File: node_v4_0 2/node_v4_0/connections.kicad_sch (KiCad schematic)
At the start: 11 parts, among them J4 Conn_02x08_Odd_Even, J5 Conn_02x02_Odd_Even, J6 GNSS_ANT, J7 RF_ANT

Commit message: most routing done
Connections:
- net GP6 renamed GP27
- net GP7 renamed GP28
- net GP8 renamed GP29
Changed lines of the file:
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@@
 		)
 	)
-	(global_label "GP7"
+	(global_label "SCL"
+		(shape input)
+		(at 120.65 107.95 0)
+		(fields_autoplaced yes)
+		(effects
+			(font
+				(size 1.27 1.27)
+			)
+			(justify left)
+		)
+		(property "Intersheetrefs" "${INTERSHEET_REFS}"
+			(at 127.1428 107.95 0)
+			(effects
+				(font
+					(size 1.27 1.27)
+				)
+				(justify left)
+				(hide yes)
+			)
+		)
+	)
+	(global_label "MOSI"
+		(shape input)
+		(at 105.41 100.33 180)
+		(fields_autoplaced yes)
+		(effects
+			(font
+				(size 1.27 1.27)
+			)
+			(justify right)
+		)
+		(property "Intersheetrefs" "${INTERSHEET_REFS}"
+			(at 97.8286 100.33 0)
+			(effects
+				(font
+					(size 1.27 1.27)
+				)
+				(justify right)
+				(hide yes)
+			)
+		)
+	)
+	(global_label "SWD"
+		(shape input)
+		(at 105.41 64.77 180)
+		(fields_autoplaced yes)
+		(effects
+			(font
+				(size 1.27 1.27)
+			)
+			(justify right)
+		)
+		(property "Intersheetrefs" "${INTERSHEET_REFS}"
+			(at 98.4939 64.77 0)
+			(effects
+				(font
+					(size 1.27 1.27)
+				)
+				(justify right)
+				(hide yes)
+			)
+		)
+	)
+	(global_label "MISO"
+		(shape input)
+		(at 105.41 102.87 180)
+		(fields_autoplaced yes)
+		(effects
+			(font
+				(size 1.27 1.27)
+			)
+			(justify right)
+		)
+		(property "Intersheetrefs" "${INTERSHEET_REFS}"
+			(at 97.8286 102.87 0)
+			(effects
+				(font
+					(size 1.27 1.27)
+				)
+				(justify right)
+				(hide yes)
+			)
+		)
+	)
+	(global_label "GNSS_ANT"
+		(shape input)
+		(at 185.42 78.74 180)
+		(fields_autoplaced yes)
+		(effects
+			(font
+				(size 1.27 1.27)
+			)
+			(justify right)
+		)
+		(property "Intersheetrefs" "${INTERSHEET_REFS}"
+			(at 173.061 78.74 0)
+			(effects
+				(font
+					(size 1.27 1.27)
+				)
+				(justify right)
+				(hide yes)
+			)
+		)
+	)
+	(global_label "SPI_CS"
+		(shape input)
+		(at 105.41 107.95 180)
+		(fields_autoplaced yes)
+		(effects
+			(font
+				(size 1.27 1.27)
+			)
+			(justify right)
+		)
+		(property "Intersheetrefs" "${INTERSHEET_REFS}"
+			(at 95.8934 107.95 0)
+			(effects
+				(font
+					(size 1.27 1.27)
+				)
+				(justify right)
+				(hide yes)
+			)
+		)
+	)
+	(global_label "RF_ANT"
+		(shape input)
+		(at 196.85 121.92 180)
+		(fields_autoplaced yes)
+		(effects
+			(font
+				(size 1.27 1.27)
+			)
+			(justify right)
+		)
+		(property "Intersheetrefs" "${INTERSHEET_REFS}"
+			(at 187.1519 121.92 0)
+			(effects
+				(font
+					(size 1.27 1.27)
+				)
+				(justify right)
+				(hide yes)
+			)
+		)
+	)
+	(global_label "TX1"
+		(shape input)
+		(at 105.41 95.25 180)
+		(fields_autoplaced yes)
+		(effects
+			(font
+				(size 1.27 1.27)
+			)
+			(justify right)
+		)
+		(property "Intersheetrefs" "${INTERSHEET_REFS}"
+			(at 99.0382 95.25 0)
+			(effects
+				(font
+					(size 1.27 1.27)
+				)
+				(justify right)
+				(hide yes)
+			)
+		)
+	)
+	(global_label "GP28"
 		(shape input)
 		(at 120.65 100.33 0)
@@
 		)
 		(property "Intersheetrefs" "${INTERSHEET_REFS}"
-			(at 127.3847 100.33 0)
-			(effects
-				(font
-					(size 1.27 1.27)
-				)
-				(justify left)
-				(hide yes)
-			)
-		)
-	)
-	(global_label "GP6"
+			(at 128.5942 100.33 0)
+			(effects
+				(font
+					(size 1.27 1.27)
+				)
+				(justify left)
+				(hide yes)
+			)
+		)
+	)
+	(global_label "GP29"
+		(shape input)
+		(at 120.65 102.87 0)
+		(fields_autoplaced yes)
+		(effects
+			(font
+				(size 1.27 1.27)
+			)
+			(justify left)
+		)
+		(property "Intersheetrefs" "${INTERSHEET_REFS}"
+			(at 128.5942 102.87 0)
+			(effects
+				(font
+					(size 1.27 1.27)
+				)
+				(justify left)
+				(hide yes)
+			)
+		)
+	)
+	(global_label "SDA"
+		(shape input)
+		(at 120.65 105.41 0)
+		(fields_autoplaced yes)
+		(effects
+			(font
+				(size 1.27 1.27)
+			)
+			(justify left)
+		)
+		(property "Intersheetrefs" "${INTERSHEET_REFS}"
+			(at 127.2033 105.41 0)
+			(effects
+				(font
+					(size 1.27 1.27)
+				)
+				(justify left)
+				(hide yes)
+			)
+		)
+	)
+	(global_label "GP27"
 		(shape input)
 		(at 120.65 97.79 0)
@@
 		)
 		(property "Intersheetrefs" "${INTERSHEET_REFS}"
-			(at 127.3847 97.79 0)
-			(effects
-				(font
-					(size 1.27 1.27)
-				)
-				(justify left)
-				(hide yes)
-			)
-		)
-	)
-	(global_label "SCL"
-		(shape input)
-		(at 120.65 107.95 0)
-		(fields_autoplaced yes)
-		(effects
-			(font
-				(size 1.27 1.27)
-			)
-			(justify left)
-		)
-		(property "Intersheetrefs" "${INTERSHEET_REFS}"
-			(at 127.1428 107.95 0)
-			(effects
-				(font
-					(size 1.27 1.27)
-				)
-				(justify left)
-				(hide yes)
-			)
-		)
-	)
-	(global_label "MOSI"
-		(shape input)
-		(at 105.41 100.33 180)
-		(fields_autoplaced yes)
-		(effects
-			(font
-				(size 1.27 1.27)
-			)
-			(justify right)
-		)
-		(property "Intersheetrefs" "${INTERSHEET_REFS}"
-			(at 97.8286 100.33 0)
-			(effects
-				(font
-					(size 1.27 1.27)
-				)
-				(justify right)
-				(hide yes)
-			)
-		)
-	)
-	(global_label "SWD"
-		(shape input)
-		(at 105.41 64.77 180)
-		(fields_autoplaced yes)
-		(effects
-			(font
-				(size 1.27 1.27)
-			)
-			(justify right)
-		)
-		(property "Intersheetrefs" "${INTERSHEET_REFS}"
-			(at 98.4939 64.77 0)
-			(effects
-				(font
-					(size 1.27 1.27)
-				)
-				(justify right)
-				(hide yes)
-			)
-		)
-	)
-	(global_label "MISO"
-		(shape input)
-		(at 105.41 102.87 180)
-		(fields_autoplaced yes)
-		(effects
-			(font
-				(size 1.27 1.27)
-			)
-			(justify right)
-		)
-		(property "Intersheetrefs" "${INTERSHEET_REFS}"
-			(at 97.8286 102.87 0)
-			(effects
-				(font
-					(size 1.27 1.27)
-				)
-				(justify right)
-				(hide yes)
-			)
-		)
-	)
-	(global_label "GNSS_ANT"
-		(shape input)
-		(at 185.42 78.74 180)
-		(fields_autoplaced yes)
-		(effects
-			(font
-				(size 1.27 1.27)
-			)
-			(justify right)
-		)
-		(property "Intersheetrefs" "${INTERSHEET_REFS}"
-			(at 173.061 78.74 0)
-			(effects
-				(font
-					(size 1.27 1.27)
-				)
-				(justify right)
-				(hide yes)
-			)
-		)
-	)
-	(global_label "SPI_CS"
-		(shape input)
-		(at 105.41 107.95 180)
-		(fields_autoplaced yes)
-		(effects
-			(font
-				(size 1.27 1.27)
-			)
-			(justify right)
-		)
-		(property "Intersheetrefs" "${INTERSHEET_REFS}"
-			(at 95.8934 107.95 0)
-			(effects
-				(font
-					(size 1.27 1.27)
-				)
-				(justify right)
-				(hide yes)
-			)
-		)
-	)
-	(global_label "RF_ANT"
-		(shape input)
-		(at 196.85 121.92 180)
-		(fields_autoplaced yes)
-		(effects
-			(font
-				(size 1.27 1.27)
-			)
-			(justify right)
-		)
-		(property "Intersheetrefs" "${INTERSHEET_REFS}"
-			(at 187.1519 121.92 0)
-			(effects
-				(font
-					(size 1.27 1.27)
-				)
-				(justify right)
-				(hide yes)
-			)
-		)
-	)
-	(global_label "TX1"
-		(shape input)
-		(at 105.41 95.25 180)
-		(fields_autoplaced yes)
-		(effects
-			(font
-				(size 1.27 1.27)
-			)
-			(justify right)
-		)
-		(property "Intersheetrefs" "${INTERSHEET_REFS}"
-			(at 99.0382 95.25 0)
-			(effects
-				(font
-					(size 1.27 1.27)
-				)
-				(justify right)
-				(hide yes)
-			)
-		)
-	)
-	(global_label "GP8"
-		(shape input)
-		(at 120.65 102.87 0)
-		(fields_autoplaced yes)
-		(effects
-			(font
-				(size 1.27 1.27)
-			)
-			(justify left)
-		)
-		(property "Intersheetrefs" "${INTERSHEET_REFS}"
-			(at 127.3847 102.87 0)
-			(effects
-				(font
-					(size 1.27 1.27)
-				)
-				(justify left)
-				(hide yes)
-			)
-		)
-	)
-	(global_label "SDA"
-		(shape input)
-		(at 120.65 105.41 0)
-		(fields_autoplaced yes)
-		(effects
-			(font
-				(size 1.27 1.27)
-			)
-			(justify left)
-		)
-		(property "Intersheetrefs" "${INTERSHEET_REFS}"
-			(at 127.2033 105.41 0)
-			(effects
-				(font
+			(at 128.5942 97.79 0)
+			(effects
+				(font

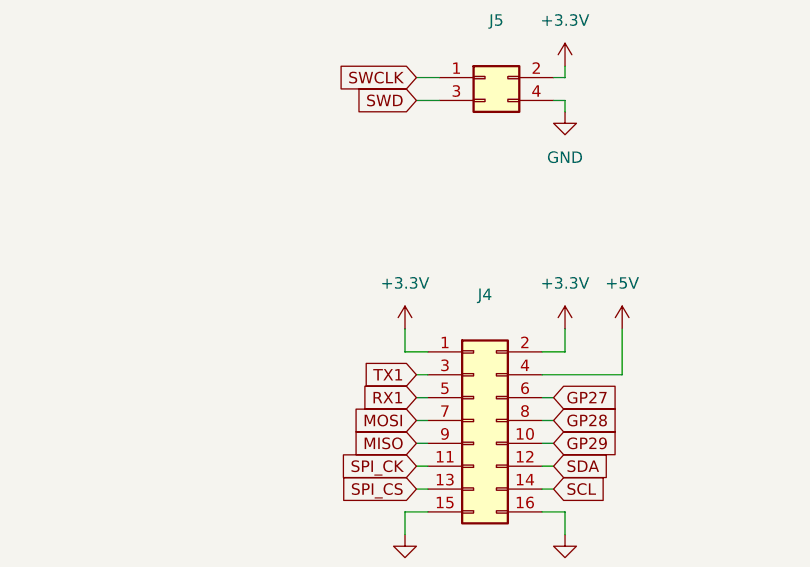
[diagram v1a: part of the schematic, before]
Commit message: added vin for solar/charge, more minor fixes
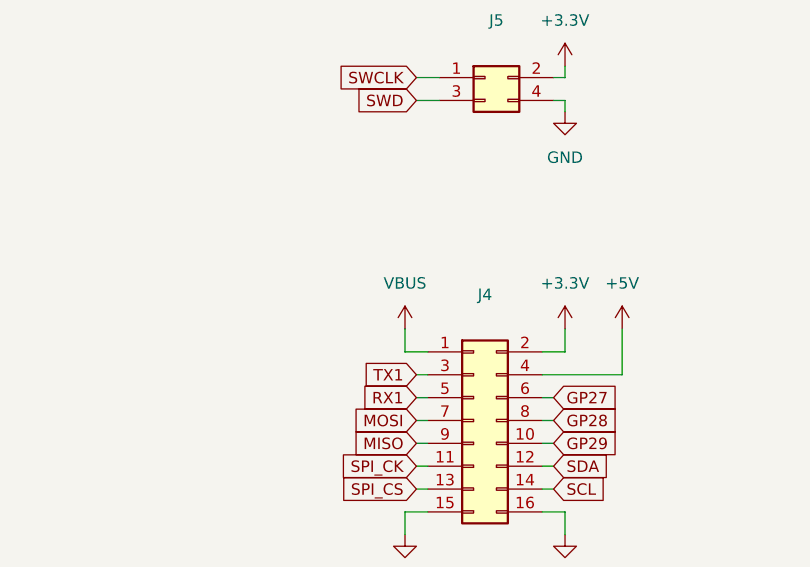
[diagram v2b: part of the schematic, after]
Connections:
- net +3.3V: no longer J4.1 (Pin_1)
- new net VBUS: J4.1 (Pin_1)
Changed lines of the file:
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@@
+	)
+	(symbol
+		(lib_id "power:VBUS")
+		(at 104.14 90.17 0)
+		(unit 1)
+		(exclude_from_sim no)
+		(in_bom yes)
+		(on_board yes)
+		(dnp no)
+		(fields_autoplaced yes)
+		(property "Reference" "#PWR055"
+			(at 104.14 93.98 0)
+			(effects
+				(font
+					(size 1.27 1.27)
+				)
+				(hide yes)
+			)
+		)
+		(property "Value" "VBUS"
+			(at 104.14 85.09 0)
+			(effects
+				(font
+					(size 1.27 1.27)
+				)
+			)
+		)
+		(property "Footprint" ""
+			(at 104.14 90.17 0)
+			(effects
+				(font
+					(size 1.27 1.27)
+				)
+				(hide yes)
+			)
+		)
+		(property "Datasheet" ""
+			(at 104.14 90.17 0)
+			(effects
+				(font
+					(size 1.27 1.27)
+				)
+				(hide yes)
+			)
+		)
+		(property "Description" "Power symbol creates a global label with name \"VBUS\""
+			(at 104.14 90.17 0)
+			(effects
+				(font
+					(size 1.27 1.27)
+				)
+				(hide yes)
+			)
+		)
+		(pin "1"
+		)
+		(instances
+			(project "node_v4_0"
+				(path "/03dc898e-8f05-4377-b5c6-8a0f09836da8/acf22234-ba16-4d6b-83f4-1166d3ac6600"
+					(reference "#PWR055")
+					(unit 1)
+				)
+			)
+		)
 	)
 	(symbol
@@
 					(unit 1)
 				)
-			)
-		)
-	)
-	(symbol
-		(lib_id "power:+3.3V")
-		(at 104.14 90.17 0)
-		(unit 1)
-		(exclude_from_sim no)
-		(in_bom yes)
-		(on_board yes)
-		(dnp no)
-		(fields_autoplaced yes)
-		(property "Reference" "#PWR055"
-			(at 104.14 93.98 0)
-			(effects
-				(font
-					(size 1.27 1.27)
-				)
-				(hide yes)
-			)
-		)
-		(property "Value" "+3.3V"
-			(at 104.14 85.09 0)
-			(effects
-				(font
-					(size 1.27 1.27)
-				)
-			)
-		)
-		(property "Footprint" ""
-			(at 104.14 90.17 0)
-			(effects
-				(font
-					(size 1.27 1.27)
-				)
-				(hide yes)
-			)
-		)
-		(property "Datasheet" ""
-			(at 104.14 90.17 0)
-			(effects
-				(font
-					(size 1.27 1.27)
-				)
-				(hide yes)
-			)
-		)
-		(property "Description" "Power symbol creates a global label with name \"+3.3V\""
-			(at 104.14 90.17 0)
-			(effects
-				(font
-					(size 1.27 1.27)
-				)
-				(hide yes)
-			)
-		)
-		(pin "1"
-		)
-		(instances
-			(project "node_v4_0"
-				(path "/03dc898e-8f05-4377-b5c6-8a0f09836da8/acf22234-ba16-4d6b-83f4-1166d3ac6600"
-					(reference "#PWR055")
-					(unit 1)
-				)

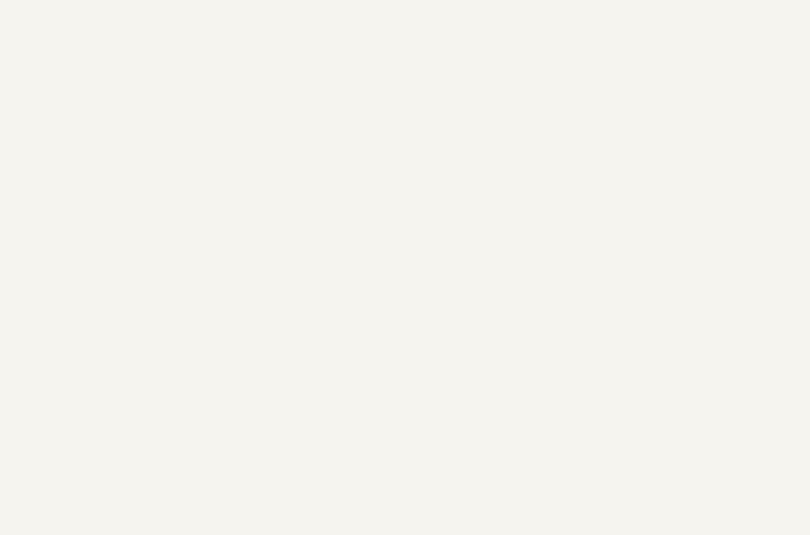
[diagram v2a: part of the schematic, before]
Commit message: moved reset button to make space for vin jst connector
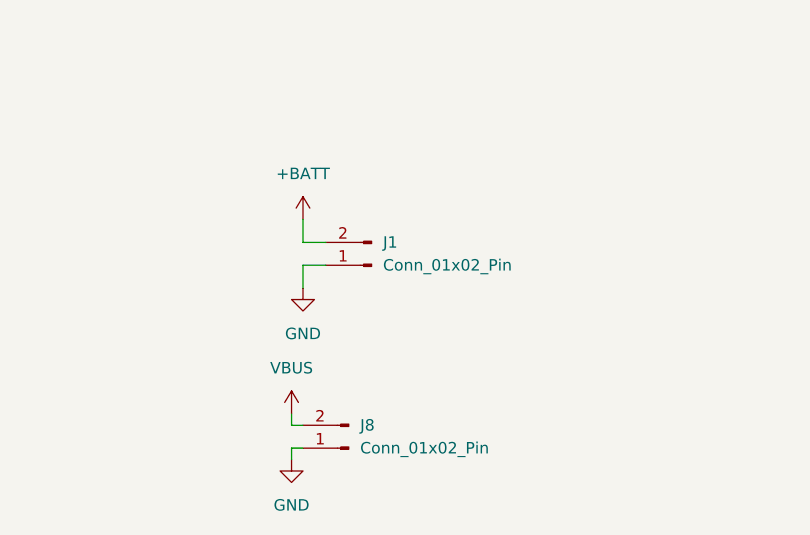
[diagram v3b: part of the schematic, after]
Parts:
- added J1, J8: Conn_01x02_Pin, Connector_JST:JST_PH_B2B-PH-K_1x02_P2.00mm_Vertical, symbol Connector:Conn_01x02_Pin
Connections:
- net GND: now also J1.1 (Pin_1), J8.1 (Pin_1)
- net VBUS: now also J8.2 (Pin_2)
- new net +BATT: J1.2 (Pin_2)
